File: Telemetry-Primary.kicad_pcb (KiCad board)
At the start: 2 copper layers, 94.5 x 82 mm, 148 parts, among them J1 CAN_LogicAnalyzer, J10 SMAConn, J11 USB_B_Micro, J12 CAN_In, J13 CAN_Out, J2 IMU_LogicAnalyzer, J3 GPS_LogicAnalyzer, J5 SDCard_LogicAnalyzer, J6 SWD, J7 PowerConn, J8 RJ45_Abracon_ARJP11A-MASA-B-A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, J9 Micro_SD_Card_Det, SW1 Reset, SW2 RTCC_BattCheck, SW3 GPS_BattCheck, U1 STM32F429ZITx, U10 ADM3055E, U11 CDSOT23-T24CAN, U2 RI3-1205S, U3 NCP1117-3.3_SOT223, U4 LAN8742A-CZ-TR, U5 USBLC6-4SC6, U7 MTK3339, U8 BNO055, U9 CP2102N-A01-GQFN24, Y1 8M, Y2 25M, Y3 32.768k

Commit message: neatening things up
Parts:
- J10: footprint Connector_Coaxial:SMA_Amphenol_132203-12_Horizontal -> UTSVT_Connectors:SMA_Amphenol_132203-12_Horizontal
- J9: footprint Connector_Card:microSD_HC_Hirose_DM3AT-SF-PEJM5 -> UTSVT_Connectors:microSD_HC_Hirose_DM3AT-SF-PEJM5
- moved C48 1.38 mm to (98.6, 52.2)
- moved U11 1.05 mm to (85.9, 53.9)
- moved SW1 0.49 mm to (78.5, 99.4)
- moved C38 0.48 mm to (112.1, 68.3)
- moved R15 0.20 mm to (105.0, 107.5)
- moved R11 0.05 mm to (107.2, 107.5)
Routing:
- net GND: track 136.2 -> 125.2 mm, vias 33 -> 36
- net /RMII_MDC: track 36.3 -> 25.6 mm
- net /RMII_TXD0: track 54.6 -> 49.4 mm
- net /RMII_TX_EN: track 55.1 -> 50.0 mm
- net Net-(J12-GND): track 56.4 -> 52.6 mm
- net /CAN/CAN_H: track 66.7 -> 63.8 mm
- net +3.3V: track 352.7 -> 354.2 mm, vias 30 -> 29
- net Net-(J12-5V): track 55.5 -> 54.8 mm
- net Net-(U1-PH1): track 12.4 -> 13.1 mm
- net Net-(U1-PH0): track 14.1 -> 14.7 mm
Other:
- board text added: "*"
- board text added: "Jump if end of bus"
- board text added: "RTC Battery Check"

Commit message: bom, gerbers, edge cuts, footprint verification
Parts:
- moved H4 0.51 mm to (163.1, 123.9)
- moved H3 0.51 mm to (163.1, 48.0)
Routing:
- net +3.3V: track 354.2 -> 349.8 mm
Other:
- board size 94.5 x 82 mm -> 95 x 82 mm

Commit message: sch and pcb pdfs
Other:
- board text added: "4 M3 Holes"
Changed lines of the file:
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@@
     )
   )
+  (gr_line (start 157.82 45.38) (end 157.82 29.5148)
+    (stroke (width 0.12) (type default)) (layer "F.SilkS"))
   (gr_line (start 94.7928 101.2952) (end 105.6132 90.4748)
     (stroke (width 0.12) (type solid)) (layer "F.SilkS"))
@@
   (gr_line (start 96.0628 102.362) (end 112.4204 102.362)
     (stroke (width 0.12) (type solid)) (layer "F.SilkS"))
+  (gr_line (start 149.5044 29.5148) (end 157.82 29.5148)
+    (stroke (width 0.12) (type default)) (layer "F.SilkS"))
   (gr_line (start 86.0044 65.532) (end 72.39 65.532)
     (stroke (width 0.12) (type solid)) (layer "F.SilkS"))
@@
   (gr_line (start 86.0044 65.532) (end 110.9472 90.4748)
     (stroke (width 0.12) (type solid)) (layer "F.SilkS"))
+  (gr_line (start 149.52 45.38) (end 149.52 29.5148)
+    (stroke (width 0.12) (type default)) (layer "F.SilkS"))
   (gr_line (start 128.8796 110.998) (end 112.4204 110.998)
     (stroke (width 0.12) (type solid)) (layer "F.SilkS"))
@@
   (gr_text "A8" (at 143.764 81.026) (layer "F.SilkS")
     (effects (font (size 1 1) (thickness 0.15)))
+  )
+  (gr_text "4 M3 Holes" (at 61.214 46.0248) (layer "Cmts.User")
+    (effects (font (size 1 1) (thickness 0.15)) (justify left bottom))
+  )
+  (dimension (type aligned) (layer "Cmts.User")
+    (pts (xy 74.168 124.7648) (xy 74.168 108.212))
+    (height -11.9888)
+    (gr_text "16.5528 mm" (at 60.383695 115.842895 90) (layer "Cmts.User")
+      (effects (font (size 1 1) (thickness 0.15)))
+    )
+    (format (prefix "") (suffix "") (units 3) (units_format 1) (precision 4))
+    (style (thickness 0.1) (arrow_length 1.27) (text_position_mode 2) (extension_height 0.58642) (extension_offset 0.5) keep_text_aligned)
   )
   (dimension (type aligned) (layer "Cmts.User")
@@
   )
   (dimension (type aligned) (layer "Cmts.User")
+    (pts (xy 157.82 45.38) (xy 149.52 45.38))
+    (height 9.312)
+    (gr_text "8.3 mm" (at 153.67 34.918) (layer "Cmts.User")
+      (effects (font (size 1 1) (thickness 0.15)))
+    )
+    (format (prefix "") (suffix "") (units 3) (units_format 1) (precision 1))
+    (style (thickness 0.1) (arrow_length 1.27) (text_position_mode 0) (extension_height 0.58642) (extension_offset 0.5) keep_text_aligned)
+  )
+  (dimension (type aligned) (layer "Cmts.User")
+    (pts (xy 163.072 44.958) (xy 163.072 126.958))
+    (height -14.8804)
+    (gr_text "82.0000 mm" (at 176.8024 85.958 90) (layer "Cmts.User")
+      (effects (font (size 1 1) (thickness 0.15)))
+    )
+    (format (prefix "") (suffix "") (units 3) (units_format 1) (precision 4))
+    (style (thickness 0.1) (arrow_length 1.27) (text_position_mode 0) (extension_height 0.58642) (extension_offset 0.5) keep_text_aligned)
+  )
+  (dimension (type aligned) (layer "Cmts.User")
     (pts (xy 163.072001 48.005999) (xy 163.068 123.9012))
     (height -9.413308)
@@
   )
   (dimension (type aligned) (layer "Cmts.User")
+    (pts (xy 71.12 123.91) (xy 66.956 123.91))
+    (height -6.0872)
+    (gr_text "4.1640 mm" (at 69.038 131.9784) (layer "Cmts.User")
+      (effects (font (size 1 1) (thickness 0.15)))
+    )
+    (format (prefix "") (suffix "") (units 3) (units_format 1) (precision 4))
+    (style (thickness 0.1) (arrow_length 1.27) (text_position_mode 2) (extension_height 0.58642) (extension_offset 0.5) keep_text_aligned)
+  )
+  (dimension (type aligned) (layer "Cmts.User")
     (pts (xy 163.072001 48.005999) (xy 74.168 48.006))
     (height 8.003258)
@@
     (style (thickness 0.1) (arrow_length 1.27) (text_position_mode 0) (extension_height 0.58642) (extension_offset 0.5) keep_text_aligned)
   )
+  (dimension (type aligned) (layer "Cmts.User")
+    (pts (xy 157.82 45.38) (xy 166.12 45.38))
+    (height -9.312)
+    (gr_text "8.3 mm" (at 161.97 34.918) (layer "Cmts.User")
+      (effects (font (size 1 1) (thickness 0.15)))
+    )
+    (format (prefix "") (suffix "") (units 3) (units_format 1) (precision 1))
+    (style (thickness 0.1) (arrow_length 1.27) (text_position_mode 0) (extension_height 0.58642) (extension_offset 0.5) keep_text_aligned)
+  )
+  (dimension (type aligned) (layer "Cmts.User")
+    (pts (xy 157.82 29.5148) (xy 157.82 44.958))
+    (height -20.1324)
+    (gr_text "15.4432 mm" (at 176.8024 37.2364 90) (layer "Cmts.User")
+      (effects (font (size 1 1) (thickness 0.15)))
+    )
+    (format (prefix "") (suffix "") (units 3) (units_format 1) (precision 4))
+    (style (thickness 0.1) (arrow_length 1.27) (text_position_mode 0) (extension_height 0.58642) (extension_offset 0.5) keep_text_aligned)
+  )
+  (dimension (type aligned) (layer "Cmts.User")
+    (pts (xy 71.12 48.006) (xy 166.12 48.006))
+    (height -20.5232)
+    (gr_text "95.0000 mm" (at 118.62 26.3328) (layer "Cmts.User")
+      (effects (font (size 1 1) (thickness 0.15)))
+    )
+    (format (prefix "") (suffix "") (units 3) (units_format 1) (precision 4))
+    (style (thickness 0.1) (arrow_length 1.27) (text_position_mode 0) (extension_height 0.58642) (extension_offset 0.5) keep_text_aligned)
+  )
+  (dimension (type aligned) (layer "Cmts.User")
+    (pts (xy 74.168 126.958) (xy 74.168 124.713999))
+    (height -11.9888)
+    (gr_text "2.2440 mm" (at 60.394151 126.956249 90) (layer "Cmts.User")
+      (effects (font (size 1 1) (thickness 0.15)))
+    )
+    (format (prefix "") (suffix "") (units 3) (units_format 1) (precision 4))
+    (style (thickness 0.1) (arrow_length 1.27) (text_position_mode 2) (extension_height 0.58642) (extension_offset 0.5) keep_text_aligned)
+  )
   (segment (start 121.350672 73.914) (end 120.82799 74.436682) (width 0.254) (layer "F.Cu") (net 1))

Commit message: schematic organization
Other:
- board text added: "UTSVT - Telemetry Leader v2.1 Fall 2021 Design by Sijin Woo and Chase Block"
- board text removed: "UTSVT - Telemetry Leader v2.2 Summer 2023 Design by Sijin Woo and Chase Block"
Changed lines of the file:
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@@
     (effects (font (size 1 1) (thickness 0.15)))
   )
-  (gr_text "UTSVT - Telemetry \nLeader v2.2\nSummer 2023\n\nDesign by Sijin Woo\nand Chase Block" (at 155.8 113.4) (layer "F.SilkS")
+  (gr_text "UTSVT - Telemetry \nLeader v2.1\nFall 2021\n\nDesign by Sijin Woo\nand Chase Block" (at 155.8 113.4) (layer "F.SilkS")
     (effects (font (size 1 1) (thickness 0.15)))
   )

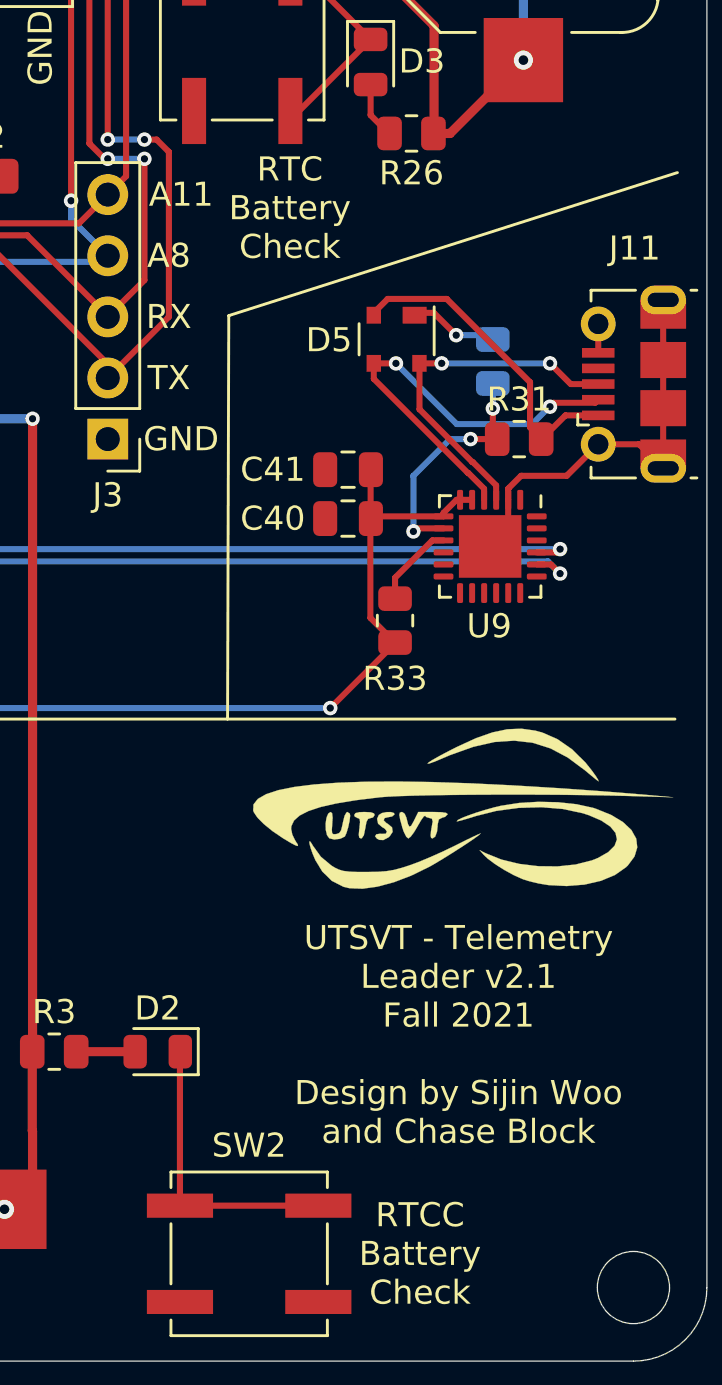
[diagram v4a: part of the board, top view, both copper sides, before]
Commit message: rename pdfs, ibom
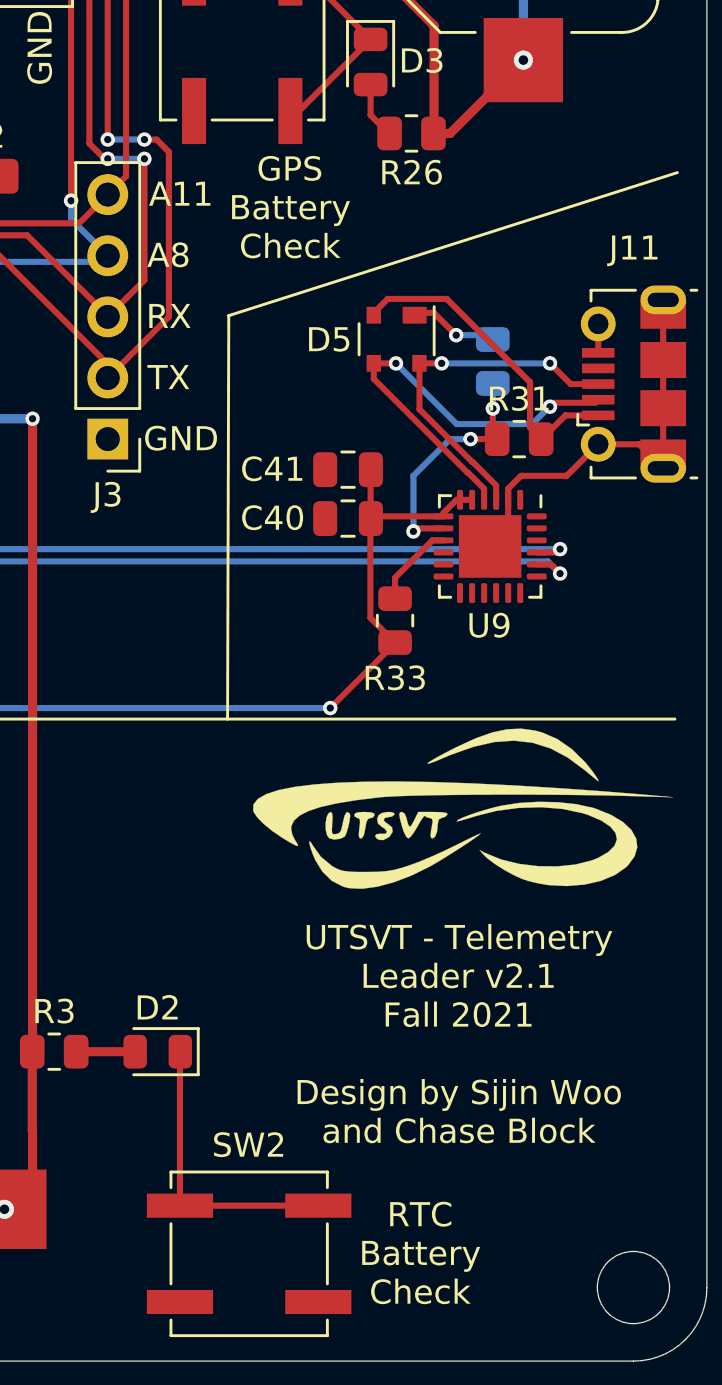
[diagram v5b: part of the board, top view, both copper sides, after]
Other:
- board text added: "GPS Battery Check"
- board text removed: "RTCC Battery Check"
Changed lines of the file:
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@@
     (effects (font (size 1 1) (thickness 0.15)))
   )
-  (gr_text "RTC\nBattery\nCheck" (at 148.7932 79.0448) (layer "F.SilkS")
+  (gr_text "GPS\nBattery\nCheck" (at 148.7932 79.0448) (layer "F.SilkS")
     (effects (font (size 1 1) (thickness 0.15)))
   )
@@
     (effects (font (size 1 1) (thickness 0.15)))
   )
-  (gr_text "RTCC\nBattery\nCheck" (at 154.2 122.5) (layer "F.SilkS")
+  (gr_text "RTC\nBattery\nCheck" (at 154.2 122.5) (layer "F.SilkS")
     (effects (font (size 1 1) (thickness 0.15)))
   )
@@
   )
   (dimension (type aligned) (layer "Cmts.User")
-    (pts (xy 71.12 48.006) (xy 166.12 48.006))
+    (pts (xy 71.0692 53.1876) (xy 166.0692 53.1876))
     (height -20.5232)
-    (gr_text "95.0000 mm" (at 118.62 26.3328) (layer "Cmts.User")
-      (effects (font (size 1 1) (thickness 0.15)))
-    )
+    (gr_text "95.0000 mm" (at 118.5692 31.5144) (layer "Cmts.User")
+      (effects (font (size 1 1) (thickness 0.15)))
+    )

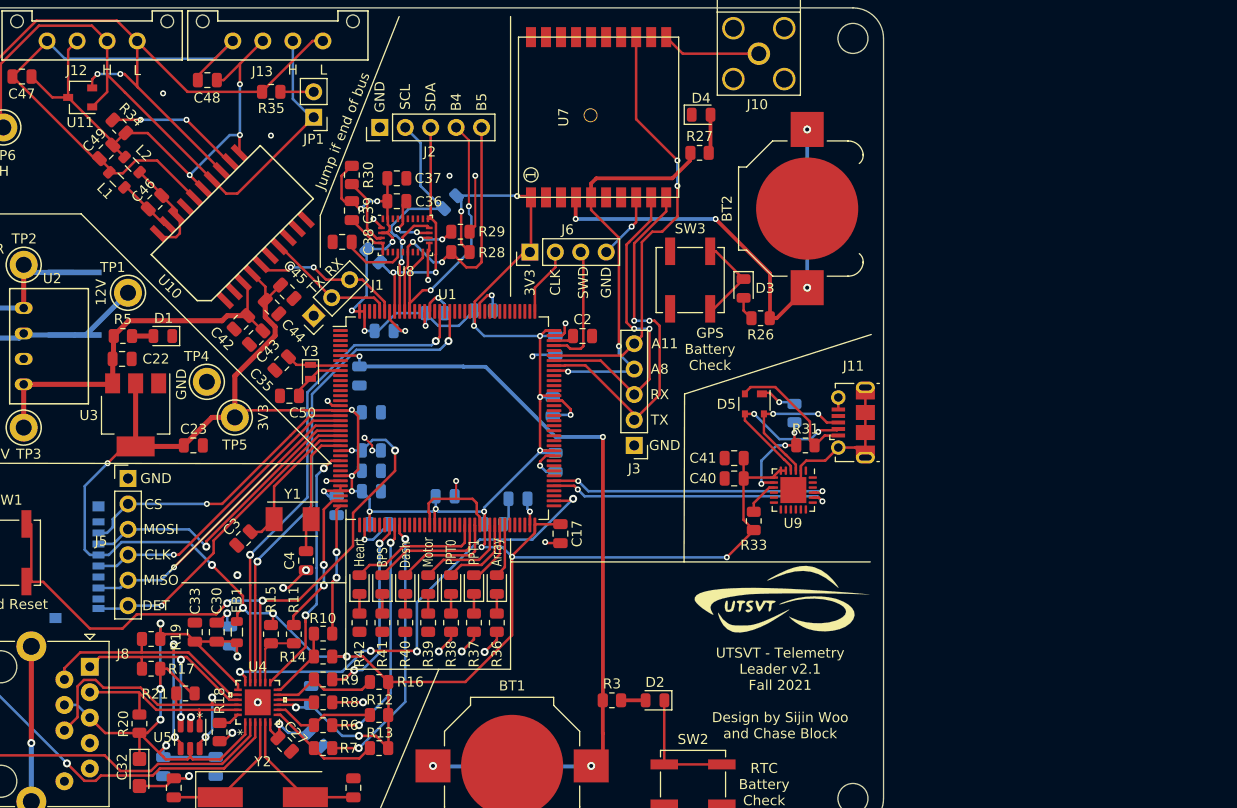
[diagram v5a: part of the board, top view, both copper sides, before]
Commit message: bluetooth schematic additions
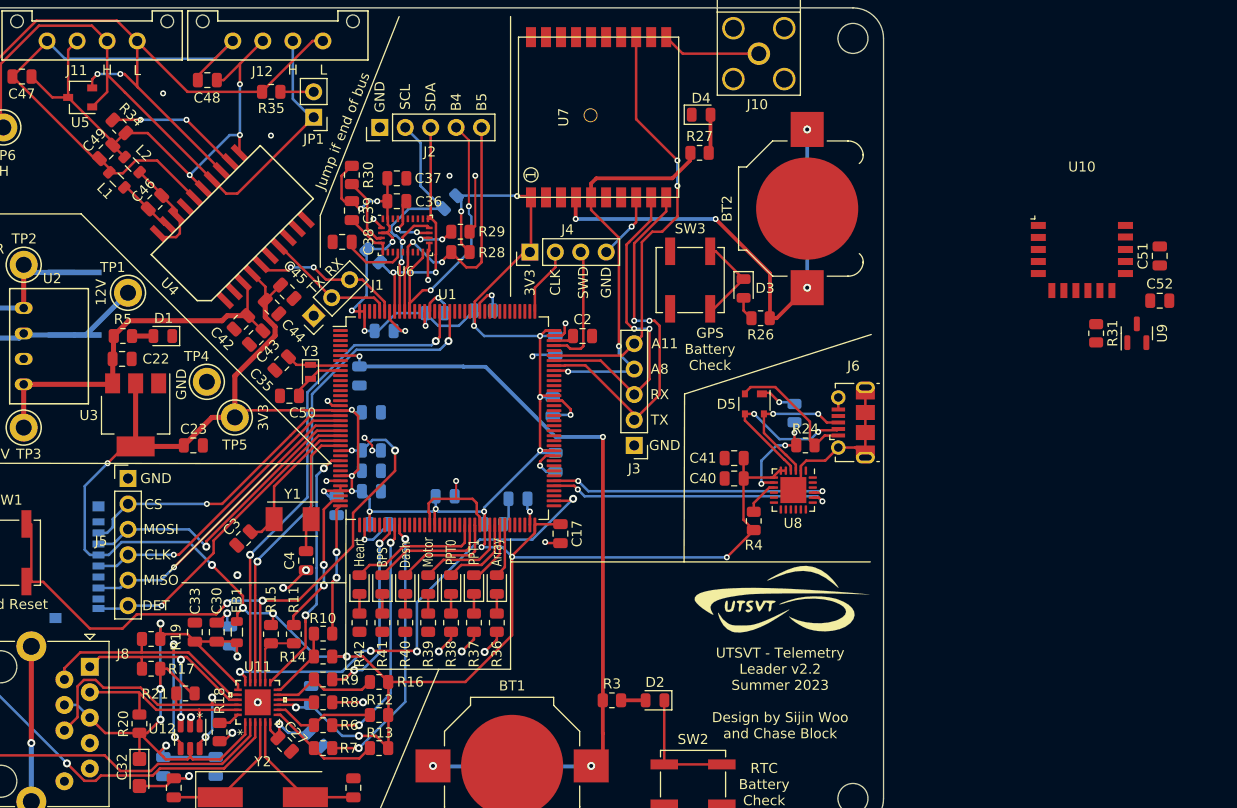
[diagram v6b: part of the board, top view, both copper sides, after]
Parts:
- added C51: 0.1u, Capacitor_SMD:C_0805_2012Metric, F.Cu at (193.7, 69.7)
- added C52: 1u, Capacitor_SMD:C_0805_2012Metric, F.Cu at (193.7, 74.2)
- added R31: 4.7k, Resistor_SMD:R_0805_2012Metric, F.Cu at (187.4, 77.4)
- added U10: RN4871-I, RF_Module:Microchip_RN4871, F.Cu at (185.9, 70.1)
- added U9: MCP112, Package_TO_SOT_SMD:SOT-23, F.Cu at (191.4, 77.4)
- C39: value 100n -> 0.1u
- U3: value NCP1117-3.3_SOT223 -> LD1117-3.3_SOT223
- U8: renamed from U9; value CP2102N-A01-GQFN24 -> CP2102N-A02-GQFN24
- renumbered J12 to J11, J13 to J12, J6 to J4, J11 to J6, R31 to R24, R32 to R25, R33 to R4, U4 to U11, U5 to U12, U10 to U4, U11 to U5, U8 to U6
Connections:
- net /PF0 renamed /I2C2_SDA
- net /PF1 renamed /I2C2_SCL
- U1 pad 1: unconnected-(U1-PE2-Pad1) -> /SPI4_CLK
- U1 pad 104: unconnected-(U1-PA12-Pad104) -> /PA12
- U1 pad 110: unconnected-(U1-PA15-Pad110) -> /SPI3_CS
- U1 pad 111: unconnected-(U1-PC10-Pad111) -> /SPI3_CLK
- U1 pad 112: unconnected-(U1-PC11-Pad112) -> /SPI3_MISO
- U1 pad 113: unconnected-(U1-PC12-Pad113) -> /SPI3_MOSI
- U1 pad 114: unconnected-(U1-PD0-Pad114) -> /PD0
- U1 pad 115: unconnected-(U1-PD1-Pad115) -> /PD1
- U1 pad 116: unconnected-(U1-PD2-Pad116) -> /PD2
- U1 pad 117: unconnected-(U1-PD3-Pad117) -> /PD3
- U1 pad 118: unconnected-(U1-PD4-Pad118) -> /PD4
- U1 pad 119: unconnected-(U1-PD5-Pad119) -> /USART2_TX
- U1 pad 122: unconnected-(U1-PD6-Pad122) -> /USART2_RX
- U1 pad 123: unconnected-(U1-PD7-Pad123) -> /PD7
- U1 pad 124: unconnected-(U1-PG9-Pad124) -> /USART6_RX
- U1 pad 125: unconnected-(U1-PG10-Pad125) -> /PG10
- U1 pad 127: unconnected-(U1-PG12-Pad127) -> /PG12
- U1 pad 129: unconnected-(U1-PG14-Pad129) -> /USART6_TX
- U1 pad 132: unconnected-(U1-PG15-Pad132) -> /PG15
- U1 pad 133: unconnected-(U1-PB3-Pad133) -> /PB3
- U1 pad 141: unconnected-(U1-PE0-Pad141) -> /UART8_RX
- U1 pad 142: unconnected-(U1-PE1-Pad142) -> /UART8_TX
- U1 pad 2: unconnected-(U1-PE3-Pad2) -> /PE3
- U1 pad 26: unconnected-(U1-PC0-Pad26) -> /PC0
- U1 pad 28: unconnected-(U1-PC2-Pad28) -> /PC2
- U1 pad 29: unconnected-(U1-PC3-Pad29) -> /PC3
- U1 pad 3: unconnected-(U1-PE4-Pad3) -> /SPI4_CS
- U1 pad 34: unconnected-(U1-PA0-Pad34) -> /WKUP
- U1 pad 37: unconnected-(U1-PA3-Pad37) -> /PA3
- U1 pad 4: unconnected-(U1-PE5-Pad4) -> /SPI4_MISO
- U1 pad 40: unconnected-(U1-PA4-Pad40) -> /PA4
- U1 pad 41: unconnected-(U1-PA5-Pad41) -> /PA5
- U1 pad 42: unconnected-(U1-PA6-Pad42) -> /PA6
- U1 pad 46: unconnected-(U1-PB0-Pad46) -> /PB0
- U1 pad 47: unconnected-(U1-PB1-Pad47) -> /PB1
- U1 pad 48: unconnected-(U1-PB2-Pad48) -> /PB2
- U1 pad 49: unconnected-(U1-PF11-Pad49) -> /PF11
- U1 pad 5: unconnected-(U1-PE6-Pad5) -> /SPI4_MOSI
- U1 pad 50: unconnected-(U1-PF12-Pad50) -> /PF12
- U1 pad 53: unconnected-(U1-PF13-Pad53) -> /PF13
- U1 pad 54: unconnected-(U1-PF14-Pad54) -> /PF14
- U1 pad 55: unconnected-(U1-PF15-Pad55) -> /PF15
- U1 pad 56: unconnected-(U1-PG0-Pad56) -> /PG0
- U1 pad 57: unconnected-(U1-PG1-Pad57) -> /PG1
- U1 pad 69: unconnected-(U1-PB10-Pad69) -> /SPI2_CLK
- U1 pad 7: unconnected-(U1-PC13-Pad7) -> /PC13
- U1 pad 70: unconnected-(U1-PB11-Pad70) -> /PB11
- U1 pad 73: unconnected-(U1-PB12-Pad73) -> /SPI2_CS
- U1 pad 75: unconnected-(U1-PB14-Pad75) -> /SPI2_MISO
- U1 pad 76: unconnected-(U1-PB15-Pad76) -> /SPI2_MOSI
- U1 pad 79: unconnected-(U1-PD10-Pad79) -> /PD10
- U1 pad 80: unconnected-(U1-PD11-Pad80) -> /PD11
- U1 pad 81: unconnected-(U1-PD12-Pad81) -> /PD12
- U1 pad 82: unconnected-(U1-PD13-Pad82) -> /PD13
- U1 pad 85: unconnected-(U1-PD14-Pad85) -> /PD14
- U1 pad 86: unconnected-(U1-PD15-Pad86) -> /PD15
- U1 pad 87: unconnected-(U1-PG2-Pad87) -> /PG2
- U1 pad 88: unconnected-(U1-PG3-Pad88) -> /PG3
- U1 pad 89: unconnected-(U1-PG4-Pad89) -> /PG4
- U1 pad 90: unconnected-(U1-PG5-Pad90) -> /PG5
- U1 pad 91: unconnected-(U1-PG6-Pad91) -> /PG6
- U1 pad 92: unconnected-(U1-PG7-Pad92) -> /PG7
- U1 pad 93: unconnected-(U1-PG8-Pad93) -> /PG8
- U1 pad 96: unconnected-(U1-PC6-Pad96) -> /PC6
- U1 pad 97: unconnected-(U1-PC7-Pad97) -> /PC7
- U1 pad 98: unconnected-(U1-PC8-Pad98) -> /PC8
- U1 pad 99: unconnected-(U1-PC9-Pad99) -> /PC9
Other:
- board text added: "UTSVT - Telemetry Leader v2.2 Summer 2023 Design by Sijin Woo and Chase Block"
- board text removed: "UTSVT - Telemetry Leader v2.1 Fall 2021 Design by Sijin Woo and Chase Block"
